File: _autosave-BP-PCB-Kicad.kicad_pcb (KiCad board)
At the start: 2 copper layers, 98 x 120.7 mm, 21 parts, among them IC1 LMT84DCKT, J10 A3C-4DA-2DSA_71_, J12 A3C-4DA-2DSA_71_, J16 DF14-15P-1.25H52, J17 DF14-30P-1.25H_35_, J18 DF14-15P-1.25H52, J19 DF14-15P-1.25H52, J20 A3C-50DA-2DSA_71_, J21 A3C-50DA-2DSA_71_, J22 A3C-50DA-2DSA_71_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

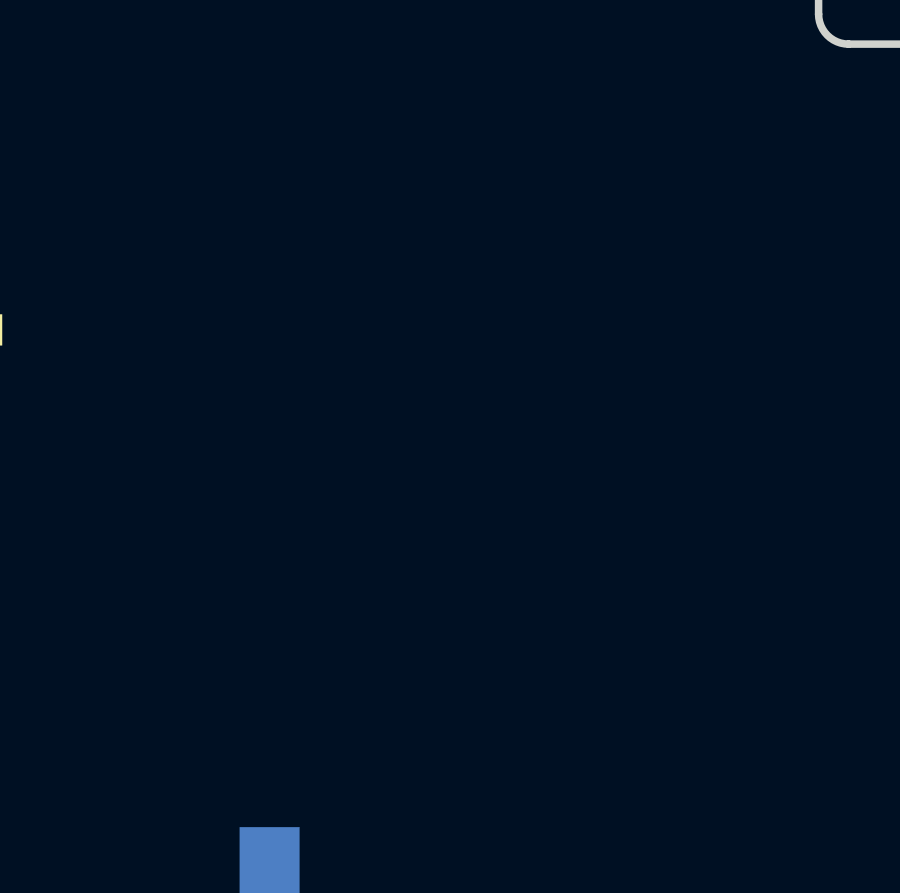
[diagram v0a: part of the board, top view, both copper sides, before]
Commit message: Added ICs to schematic
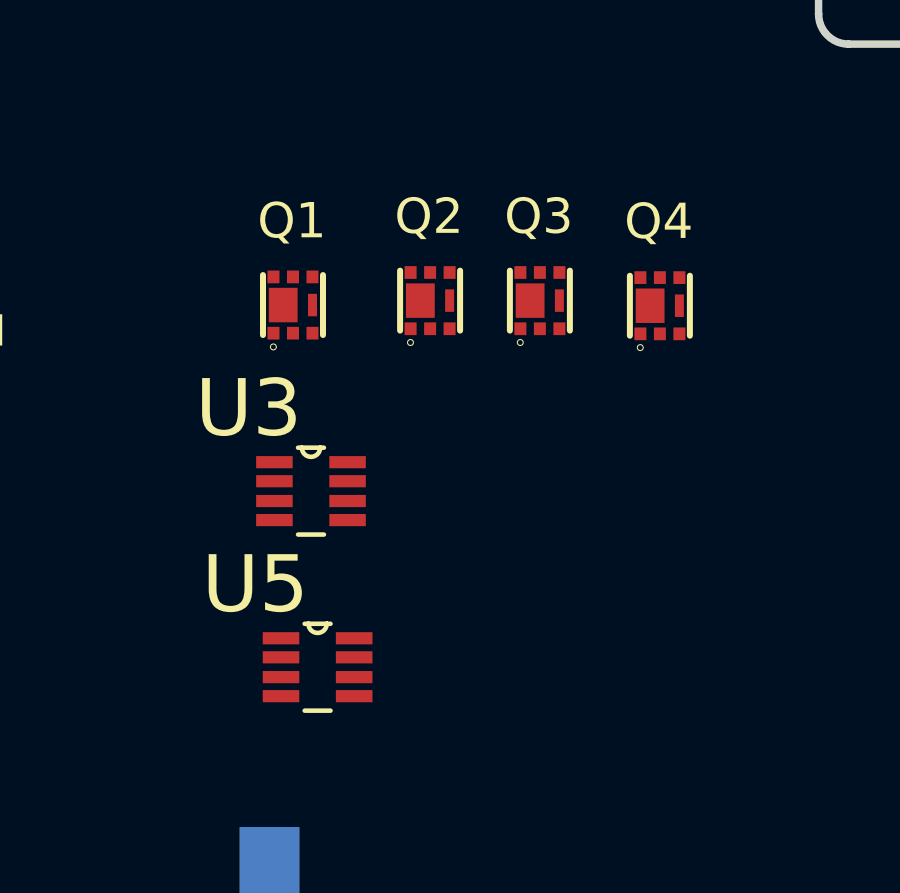
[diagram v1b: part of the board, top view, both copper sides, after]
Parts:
- added Q1: SSM6K514NU,LF, Custom-Footprints:SSM6K514NULF, F.Cu at (36.5, 53.7)
- added Q2: SSM6K514NU,LF, Custom-Footprints:SSM6K514NULF, F.Cu at (41.0, 53.5)
- added Q3: SSM6K514NU,LF, Custom-Footprints:SSM6K514NULF, F.Cu at (44.7, 53.5)
- added Q4: SSM6K514NU,LF, Custom-Footprints:SSM6K514NULF, F.Cu at (48.7, 53.7)
- added U3: LTC4361CTS8-2TRMPBF, Custom-Footprints:LTC4361HTS8, F.Cu at (37.1, 59.9)
- added U5: LTC4361CTS8-2TRMPBF, Custom-Footprints:LTC4361HTS8, F.Cu at (37.3, 65.8)
